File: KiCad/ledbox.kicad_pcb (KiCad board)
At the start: 2 copper layers, 80 x 50 mm, 132 parts, among them CON401 AVR_ISP, J201 Bus, J301 IR LED, J302 Button, J401 Power, J402 Power, J403 Power, J404 Port D, J405 Port B, J406 Port C, J407 ADC6, J408 ADC7, J501 6.5V-12V, J502 5V, SW301 Reset, SW302 Push 1, SW303 Push 2, U201 ST485C, U301 ULN2003, U401 ATMEGA88-20AU, U501 AZ1117-5.0, Y401 DNP/20MHz

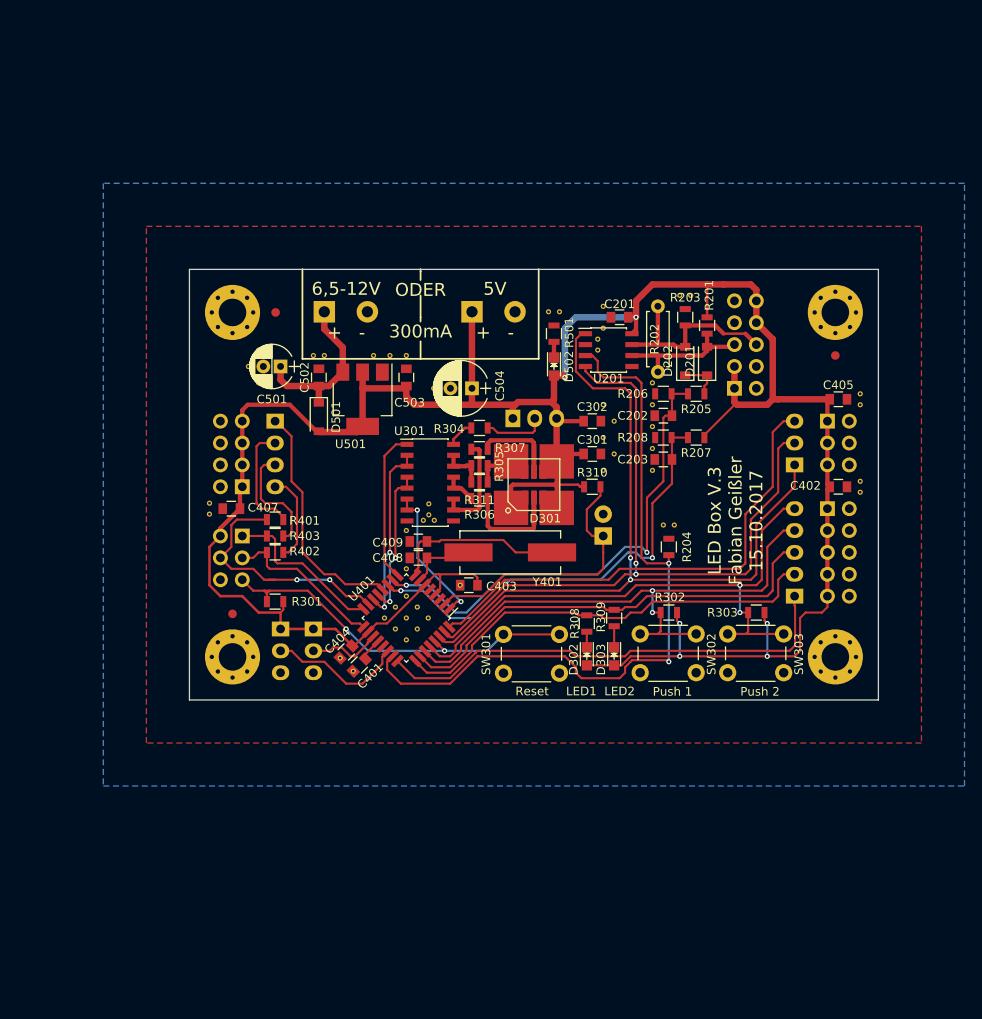
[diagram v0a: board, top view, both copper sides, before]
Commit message: Changes to V4 Schematic, new Board design
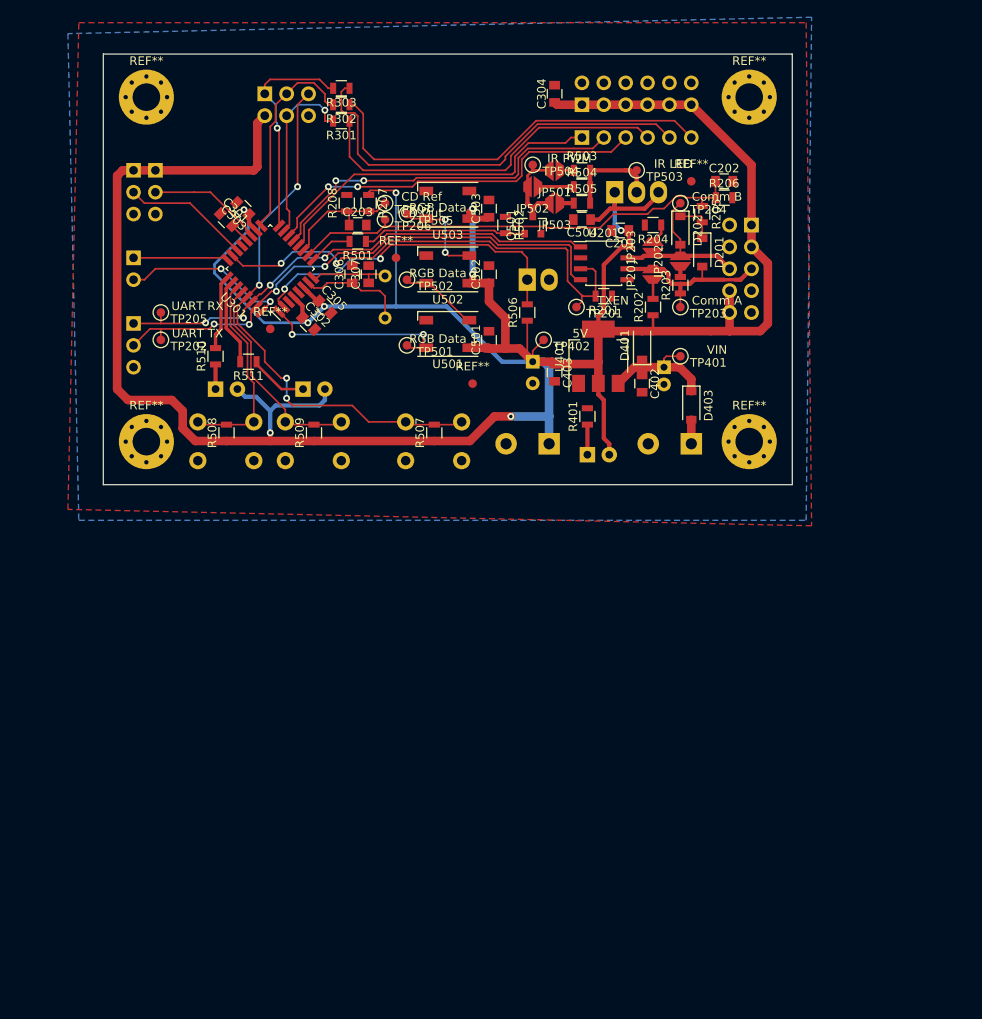
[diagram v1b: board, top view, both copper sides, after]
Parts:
- removed C405, C407: 100n, Capacitors_SMD:C_0805
- removed C408, C409: DNP/22p, Capacitors_SMD:C_0805
- removed CON401: AVR_ISP, Pin_Headers:Pin_Header_Straight_2x03
- removed D301: LRTBG6TG, ledbox-newfootprints:LED-6-BIG
- removed D302: LED1, LEDs:LED_0805
- removed D303: LED2, LEDs:LED_0805
- removed the G*** at (128.3, 101.3)
- removed the G*** at (150.0, 100.0)
- removed J403: Power, Socket_Strips:Socket_Strip_Straight_2x05
- removed J404: Port D, Socket_Strips:Socket_Strip_Straight_1x03
- removed J405: Port B, Socket_Strips:Socket_Strip_Straight_1x04
- removed J406: Port C, Socket_Strips:Socket_Strip_Straight_1x05
- removed J407: ADC6, Socket_Strips:Socket_Strip_Straight_1x03
- removed J408: ADC7, Socket_Strips:Socket_Strip_Straight_1x03
- removed R304: 150, Resistors_SMD:R_0805
- removed R305, R311: 82, Resistors_SMD:R_0805
- removed R306, R307: 22, Resistors_SMD:R_0805
- removed R308, R309: 430, Resistors_SMD:R_0805
- removed R310: 10k, Resistors_SMD:R_0805
- removed R402, R403: 1k, Resistors_SMD:R_0805
- removed the REF** at (138.4, 104.1)
- removed the REF** at (187.9, 99.6)
- removed the REF** at (187.9, 90.7)
- removed the REF** at (187.9, 89.5)
- removed the REF** at (163.8, 88.2)
- removed the REF** at (163.8, 90.7)
- removed the REF** at (163.8, 93.3)
- removed the REF** at (163.8, 95.8)
- removed the REF** at (163.8, 98.3)
- removed the REF** at (168.2, 78.0)
- removed the REF** at (166.9, 78.0)
- removed the REF** at (137.8, 102.2)
- removed the REF** at (158.0, 79.3)
- removed the REF** at (158.0, 81.8)
- removed the REF** at (153.0, 79.9)
- removed the REF** at (151.7, 79.9)
- removed the REF** at (157.4, 83.1)
- removed the REF** at (157.4, 84.4)
- removed the REF** at (158.0, 90.7)
- removed the REF** at (158.0, 98.3)
- removed the REF** at (158.0, 94.5)
- removed the REF** at (159.3, 96.4)
- removed the REF** at (137.8, 103.5)
- removed the REF** at (159.3, 92.6)
- removed the REF** at (141.4, 111.7)
- removed the REF** at (129.0, 121.7)
- removed the REF** at (127.5, 120.1)
- removed the REF** at (140.3, 86.9)
- removed the REF** at (125.7, 85.0)
- removed the REF** at (124.4, 85.0)
- removed the REF** at (135.2, 85.0)
- removed the REF** at (133.3, 85.0)
- removed the REF** at (131.4, 85.0)
- removed the REF** at (118.0, 88.2)
- removed the REF** at (138.4, 88.8)
- removed the REF** at (116.8, 86.3)
- removed the REF** at (118.0, 84.4)
- removed the REF** at (137.2, 104.1)
- removed the REF** at (135.2, 112.9)
- removed the REF** at (135.2, 105.3)
- removed the REF** at (135.2, 109.8)
- removed the REF** at (133.9, 114.2)
- removed the REF** at (136.5, 114.2)
- removed the REF** at (136.5, 116.8)
- removed the REF** at (112.3, 102.2)
- removed the REF** at (133.9, 116.8)
- removed the REF** at (135.2, 118.0)
- removed the REF** at (137.7, 115.5)
- removed the REF** at (132.6, 115.5)
- removed the REF** at (115.0, 115.0)
- removed the REF** at (185.0, 85.0)
- removed the REF** at (115.0, 80.0)
- removed the REF** at (115.0, 120.0)
- removed the REF** at (185.0, 120.0)
- removed the REF** at (185.0, 80.0)
- removed the REF** at (112.3, 103.4)
- removed the REF** at (120.0, 80.0)
- removed the REF** at (135.2, 115.5)
- removed the REF** at (166.3, 104.7)
- removed the REF** at (165.0, 104.7)
- removed the REF** at (187.9, 100.9)
- removed SW301: Reset, Buttons_Switches_THT:SW_PUSH_6mm_h5mm
- removed SW302: Push 1, Buttons_Switches_THT:SW_PUSH_6mm_h5mm
- removed SW303: Push 2, Buttons_Switches_THT:SW_PUSH_6mm_h5mm
- removed Y401: DNP/20MHz, Crystals:Crystal_HC49-SD_SMD
- added C303: 100n, Capacitors_SMD:C_0805, F.Cu at (116.2, 67.9)
- added C304: 100n, Capacitors_SMD:C_0805, F.Cu at (152.4, 54.6)
- added C305: 100n, Capacitors_SMD:C_0805, F.Cu at (125.7, 79.4)
- added C306: 22p, Capacitors_SMD:C_0805, F.Cu at (128.9, 75.6)
- added C307: 22p, Capacitors_SMD:C_0805, F.Cu at (130.8, 75.6)
- added CON301: AVR_ISP, Connectors_IDC:IDC-Header_2x03_Pitch2.54mm_Straight, B.Cu at (118.7, 54.6)
- added D401: 1N4148, Diodes_SMD:D_SOD-123, F.Cu at (162.6, 83.8)
- added D402: LED2, LEDs:LED_D3.0mm, B.Cu at (156.2, 96.5)
- added D403: PMEG4010ER, Diodes_SMD:D_SOD-123, F.Cu at (168.3, 90.8)
- added G***: LOGO, LOGO, B.Cu at (140.0, 75.0)
- added G***: LOGO, LOGO, F.Cu at (139.1, 56.5)
- added J303: Spare, Socket_Strips:Socket_Strip_Straight_1x02_Pitch2.54mm, B.Cu at (103.5, 73.7)
- added J304: UART, Socket_Strips:Socket_Strip_Straight_1x03_Pitch2.54mm, B.Cu at (103.5, 81.3)
- added J305: ADC6, Socket_Strips:Socket_Strip_Straight_1x03_Pitch2.54mm, B.Cu at (106.0, 63.5)
- added J306: ADC7, Socket_Strips:Socket_Strip_Straight_1x03_Pitch2.54mm, B.Cu at (103.5, 63.5)
- added JP201: COMMA PU, SMD_Jumper:Jumper_SMD_02, F.Cu at (163.8, 75.6)
- added JP202: TERM, SMD_Jumper:Jumper_SMD_02, F.Cu at (167.0, 74.0)
- added JP203: COMMB PD, SMD_Jumper:Jumper_SMD_02, F.Cu at (163.8, 72.4)
- added JP501: IR 12mA, SMD_Jumper:Jumper_SMD_02, F.Cu at (152.4, 63.5)
- added JP502: IR 24mA, SMD_Jumper:Jumper_SMD_02, F.Cu at (149.9, 65.4)
- added JP503: IR 48mA, SMD_Jumper:Jumper_SMD_02, F.Cu at (152.4, 67.3)
- added Q501: NTR4003N, TO_SOT_Packages_SMD:SOT-23, F.Cu at (149.9, 69.8)
- added R502: 100k, Resistors_SMD:R_0805, F.Cu at (146.7, 69.8)
- added R503: 300, Resistors_SMD:R_0805, F.Cu at (155.6, 63.5)
- added R504: 150, Resistors_SMD:R_0805, F.Cu at (155.6, 65.4)
- added R505: 75, Resistors_SMD:R_0805, F.Cu at (155.6, 67.3)
- added R506: 10k, Resistors_SMD:R_0805, F.Cu at (149.2, 80.0)
- added R507: 10k, Resistors_SMD:R_0805, F.Cu at (138.4, 94.0)
- added R508: 10k, Resistors_SMD:R_0805, F.Cu at (114.3, 94.0)
- added R509: 10k, Resistors_SMD:R_0805, F.Cu at (124.5, 94.0)
- added R510: 430, Resistors_SMD:R_0805, F.Cu at (113.0, 85.1)
- added R511: 430, Resistors_SMD:R_0805, F.Cu at (116.8, 85.7)
- added REF**: Fiducial_1mm_Dia_2mm_Outer, Fiducials:Fiducial_1mm_Dia_2mm_Outer, F.Cu at (168.3, 64.8)
- added REF**: Fiducial_1mm_Dia_2mm_Outer, Fiducials:Fiducial_1mm_Dia_2mm_Outer, F.Cu at (142.9, 88.3)
- added REF**: Fiducial_1mm_Dia_2mm_Outer, Fiducials:Fiducial_1mm_Dia_2mm_Outer, F.Cu at (119.4, 81.9)
- added REF**: Fiducial_1mm_Dia_2mm_Outer, Fiducials:Fiducial_1mm_Dia_2mm_Outer, F.Cu at (134.0, 73.7)
- added REF**: MountingHole_3.2mm_M3_Pad_Via, Mounting_Holes:MountingHole_3.2mm_M3_Pad_Via, F.Cu at (105.0, 95.0)
- added REF**: MountingHole_3.2mm_M3_Pad_Via, Mounting_Holes:MountingHole_3.2mm_M3_Pad_Via, F.Cu at (105.0, 55.0)
- added REF**: MountingHole_3.2mm_M3_Pad_Via, Mounting_Holes:MountingHole_3.2mm_M3_Pad_Via, F.Cu at (175.0, 55.0)
- added REF**: MountingHole_3.2mm_M3_Pad_Via, Mounting_Holes:MountingHole_3.2mm_M3_Pad_Via, F.Cu at (175.0, 95.0)
- added SW501: Reset, Buttons_Switches_THT:SW_PUSH_6mm_h5mm, B.Cu at (141.6, 92.7)
- added SW502: Push 1, Buttons_Switches_THT:SW_PUSH_6mm_h5mm, B.Cu at (117.5, 92.7)
- added SW503: Push 2, Buttons_Switches_THT:SW_PUSH_6mm_h5mm, B.Cu at (127.6, 92.7)
- added TP201: TXEN, Test:TEST_10, F.Cu at (154.9, 79.4)
- added TP202: UART TX, Test:TEST_10, F.Cu at (106.7, 83.2)
- added TP203: Comm A, Test:TEST_10, F.Cu at (167.0, 79.4)
- added TP204: Comm B, Test:TEST_10, F.Cu at (167.0, 67.3)
- added TP205: UART RX, Test:TEST_10, F.Cu at (106.7, 80.0)
- added TP206: CD Out, Test:TEST_10, F.Cu at (132.7, 69.2)
- added TP207: CD Ref, Test:TEST_10, F.Cu at (132.7, 67.3)
- added TP401: VIN, Test:TEST_10, F.Cu at (167.0, 85.1)
- added TP402: 5V, Test:TEST_10, F.Cu at (151.1, 83.2)
- added TP501: RGB Data 1, Test:TEST_10, F.Cu at (135.3, 83.8)
- added TP502: RGB Data 2, Test:TEST_10, F.Cu at (135.3, 76.2)
- added TP503: IR LED, Test:TEST_10, F.Cu at (161.9, 63.5)
- added TP504: IR PWM, Test:TEST_10, F.Cu at (149.9, 62.9)
- added TP505: RGB Data 3, Test:TEST_10, F.Cu at (135.3, 68.6)
- added U502: WS2812B, LEDs:LED_WS2812B-PLCC4, F.Cu at (140.0, 75.0)
- added U503: WS2812B, LEDs:LED_WS2812B-PLCC4, F.Cu at (140.0, 67.5)
- added Y301: 20MHz, Crystals:Crystal_HC49-U_Vertical, B.Cu at (132.7, 80.6)
- C301: value 10u -> 100n
- C401: value 100n -> 4u7; footprint Capacitors_SMD:C_0805 -> Capacitors_THT:CP_Radial_D5.0mm_P2.00mm; moved to B.Cu
- C404: value 100n -> 47u; footprint Capacitors_SMD:C_0805 -> Capacitors_THT:CP_Radial_D6.3mm_P2.50mm; moved to B.Cu
- C501: value 4u7 -> 10u; footprint Capacitors_THT:CP_Radial_D5.0mm_P2.00mm -> Capacitors_SMD:C_0805
- C502, C503: value 100n -> 10u
- C504: value 47u -> 100n; footprint Capacitors_THT:CP_Radial_D6.3mm_P2.50mm -> Capacitors_SMD:C_0805
- D501: value 1N4148 -> LED1; footprint Diodes_SMD:D_SOD-123 -> LEDs:LED_D3.0mm; moved to B.Cu
- D502: footprint LEDs:LED_0805 -> LEDs:LED_D3.0mm; moved to B.Cu
- J201: footprint Pin_Headers:Pin_Header_Straight_2x05 -> Connectors_IDC:IDC-Header_2x05_Pitch2.54mm_Straight
- J301: value IR LED -> Power B; footprint Pin_Headers:Pin_Header_Straight_1x03 -> Socket_Strips:Socket_Strip_Straight_2x06_Pitch2.54mm
- J302: value Button -> Port B; footprint Pin_Headers:Pin_Header_Straight_1x02 -> Socket_Strips:Socket_Strip_Straight_1x06_Pitch2.54mm
- J401: value Power -> 6.5V-12V; footprint Socket_Strips:Socket_Strip_Straight_2x03 -> TerminalBlock_MetzConnect:TerminalBlock_MetzConnect_Type055_RT01502HDWU_Pitch5.00mm
- J402: value Power -> 5V; footprint Socket_Strips:Socket_Strip_Straight_2x04 -> TerminalBlock_MetzConnect:TerminalBlock_MetzConnect_Type055_RT01502HDWU_Pitch5.00mm
- J501: value 6.5V-12V -> IR LED; footprint Connectors_Terminal_Blocks:TerminalBlock_Pheonix_MKDS1.5-2pol -> Connectors_Molex:Molex_KK-6410-03_03x2.54mm_Straight
- J502: value 5V -> Button; footprint Connectors_Terminal_Blocks:TerminalBlock_Pheonix_MKDS1.5-2pol -> Connectors_Molex:Molex_KK-6410-02_02x2.54mm_Straight
- R201: value DNP/1k -> 10k
- R202: value DNP/150 -> 1k; footprint Resistors_THT:R_Axial_DIN0207_L6.3mm_D2.5mm_P7.62mm_Horizontal -> Resistors_SMD:R_0805
- R203: value DNP/1k -> 150
- R204, R301, R302, R303: value 10k -> 1k
- R401: value 1k -> 2k2
- R501: value 430 -> 100
- U301: value ULN2003 -> ATMEGA88A-AU; footprint Housings_SOIC:SOIC-16_3.9x9.9mm_Pitch1.27mm -> Housings_QFP:TQFP-32_7x7mm_Pitch0.8mm
- U401: value ATMEGA88-20AU -> AZ1117-5.0; footprint Housings_QFP:TQFP-32_7x7mm_Pitch0.8mm -> TO_SOT_Packages_SMD:SOT-223-3_TabPin2
- U501: value AZ1117-5.0 -> WS2812B; footprint TO_SOT_Packages_SMD:SOT-223-3Lead_TabPin2 -> LEDs:LED_WS2812B-PLCC4
- moved R303 77.6 mm to (127.6, 54.0)
- moved R302 70.2 mm to (127.6, 55.9)
- moved R301 56.3 mm to (127.6, 57.8)
- moved C301 50.4 mm to (114.3, 69.2), turned to 315 degrees
- moved C401 49.5 mm to (165.1, 86.4), turned to 270 degrees
- moved R207 46.8 mm to (130.8, 67.3), turned to 270 degrees
- moved J302 46.3 mm to (155.6, 59.7), turned to 270 degrees
- moved R208 45.7 mm to (128.3, 67.3), turned to 90 degrees
- moved C203 44.7 mm to (129.5, 69.8), turned to 0 degrees
- moved C404 40.1 mm to (149.9, 85.7), turned to 270 degrees
- moved R401 38.2 mm to (156.2, 92.1), turned to 90 degrees
- moved U401 37.7 mm to (157.5, 85.1), turned to 90 degrees
- moved R204 37.4 mm to (163.8, 69.8), turned to 180 degrees
- moved J301 37.3 mm to (155.6, 55.9)
- moved J501 36.5 mm to (159.4, 66.0)
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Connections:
- C301 pad 1: +5V -> GND
- C301 pad 2: GND -> Net-(C301-Pad2)
- C401 pad 1: GND -> +12V
- C401 pad 2: Net-(C401-Pad2) -> GND
- C402 pad 1: +5V -> +12V
- C501 pad 1: +12V -> +5V
- C502 pad 1: +12V -> +5V
- D501 pad 1: +12V -> Net-(D501-Pad1)
- J301 pad 2: /Interface/IR_LED_DRV -> GND
- J302 pad 1: /Controller/BTN -> /Controller/PB0
- J302 pad 2: GND -> /Controller/PB1
- J401 pad 1: +5V -> Net-(D403-Pad2)
- J501 pad 1: +12V -> +5V
- J501 pad 2: GND -> /Interface/IR_LED_DRV
- J502 pad 1: +5V -> /Controller/BTN
- R201 pad 1: +5V -> GND
- R201 pad 2: /Bus/COMM_A -> /Bus/TX_EN
- R202 pad 1: /Bus/COMM_A -> +5V
- R202 pad 2: /Bus/COMM_B -> Net-(JP201-Pad1)
- R203 pad 1: /Bus/COMM_B -> /Bus/COMM_A
- R203 pad 2: GND -> Net-(JP202-Pad1)
- R204 pad 1: GND -> Net-(JP203-Pad2)
- R204 pad 2: /Bus/TX_EN -> GND
- R301 pad 1: +5V -> /Controller/PB3
- R301 pad 2: /Controller/~RESET -> /Controller/MOSI
- R302 pad 1: +5V -> /Controller/PB5
- R302 pad 2: /Controller/PUSH1 -> /Controller/SCK
- R303 pad 1: +5V -> /Controller/PB4
- R303 pad 2: /Controller/PUSH2 -> /Controller/MISO
- R401 pad 1: /Controller/PB3 -> Net-(D402-Pad1)
- R401 pad 2: /Controller/MOSI -> GND
- R501 pad 1: Net-(D502-Pad1) -> Net-(Q501-Pad1)
- R501 pad 2: GND -> /Controller/LED_IR
- U301 pad 1: /Controller/LED_IR -> /Controller/RGB_D
- U301 pad 10: Net-(R307-Pad2) -> /Bus/AIN0
- U301 pad 11: Net-(R307-Pad2) -> /Bus/AIN1
- U301 pad 12: Net-(R306-Pad2) -> /Controller/PB0
- U301 pad 13: Net-(R306-Pad2) -> /Controller/PB1
- U301 pad 14: Net-(R305-Pad2) -> /Controller/PB2
- U301 pad 15: Net-(R305-Pad2) -> /Controller/MOSI
- U301 pad 16: Net-(R304-Pad2) -> /Controller/MISO
- U301 pad 2: /Controller/PWM_R -> /Controller/BTN
- U301 pad 3: /Controller/PWM_R -> GND
- U301 pad 4: /Controller/PWM_G -> +5V
- U301 pad 5: /Controller/PWM_G -> GND
- U301 pad 6: /Controller/PWM_B -> +5V
- U301 pad 7: /Controller/PWM_B -> /Controller/XTAL1
- U301 pad 8: GND -> /Controller/XTAL2
- U301 pad 9: Net-(U301-Pad9) -> /Controller/LED_IR
- U401 pad 1: /Controller/PWM_B -> GND
- U401 pad 2: /Controller/BTN -> +5V
- U401 pad 3: GND -> +12V
- U501 pad 1: GND -> +5V
- U501 pad 2: +5V -> Net-(TP502-Pad1)
- U501 pad 3: +12V -> GND
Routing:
- net +5V: track 301.7 -> 373.8 mm, vias 6 -> 9
- net /Controller/PB2: track 0.00 -> 45.6 mm, vias 0 -> 2
- net /Controller/PC1: track 54.8 -> 11.0 mm
- net /Controller/PB1: track 0.00 -> 43.3 mm, vias 0 -> 2
- net /Controller/LED1: track 51.4 -> 8.75 mm
- net /Controller/PUSH2: track 66.9 -> 24.7 mm, vias 2 -> 0
- net /Controller/LED2: track 52.0 -> 10.2 mm
- net /Controller/PUSH1: track 65.3 -> 23.8 mm, vias 2 -> 0
- net /Bus/AIN1: track 52.6 -> 14.4 mm, vias 2 -> 0
- net /Controller/PD2: track 57.1 -> 19.6 mm, vias 0 -> 2
- net /Controller/PB5: track 10.4 -> 47.4 mm
- net /Controller/PB4: track 13.1 -> 49.4 mm
- net /Bus/RX: track 89.0 -> 58.6 mm, vias 2 -> 4
- net /Controller/PB3: track 13.0 -> 42.5 mm
- net /Bus/TX_EN: track 84.0 -> 56.5 mm
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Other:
- net class Default: via_dia 0.6 -> 0.8; via_drill 0.3 -> 0.4
- rule pad_to_mask_clearance: 0.2 -> 0
- board text removed: "+ -"
- board text removed: "5V"
- board text removed: "6,5-12V"
- board text removed: "LED Box V.3 Fabian Geißler 15.10.2017"
- board text removed: "LfdNr Addr Test"
- board text removed: "ODER 300mA"

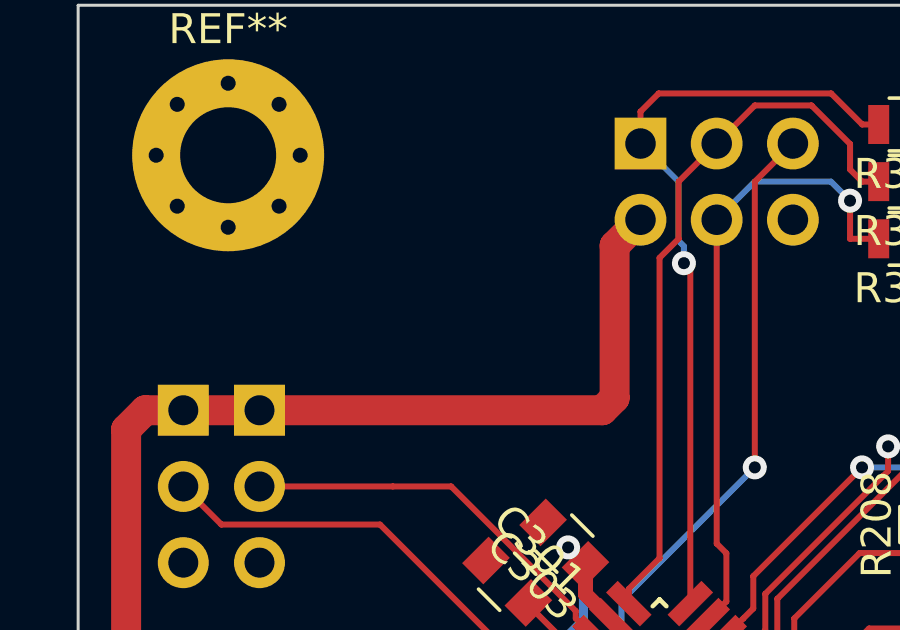
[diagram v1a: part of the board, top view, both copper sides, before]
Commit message: Added board plot
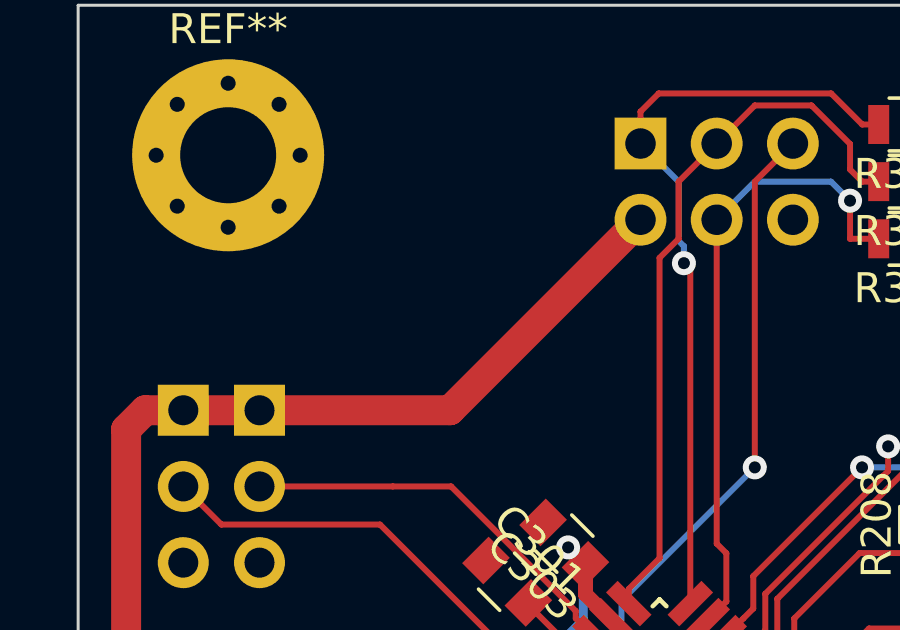
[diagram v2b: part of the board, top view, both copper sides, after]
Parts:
- moved G*** 1.07 mm to (140.0, 56.0)
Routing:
- net +5V: track 373.8 -> 370.8 mm
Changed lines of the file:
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@@
     (thickness 1.6)
     (drawings 4)
-    (tracks 595)
+    (tracks 593)
     (zones 0)
     (modules 101)
@@
   )
   (setup
-    (last_trace_width 0.2)
+    (last_trace_width 1)
     (user_trace_width 0.2)
     (user_trace_width 0.3)
@@
     (visible_elements FFFFFF7F)
     (pcbplotparams
-      (layerselection 0x010fc_ffffffff)
+      (layerselection 0x00000_ffffffff)
       (usegerberextensions false)
       (usegerberattributes true)
@@
       (padsonsilk false)
       (subtractmaskfromsilk false)
-      (outputformat 1)
+      (outputformat 4)
       (mirror false)
-      (drillshape 1)
+      (drillshape 0)
       (scaleselection 1)
-      (outputdirectory ""))
+      (outputdirectory output))
   )
   (net 0 "")
@@
   )
   (module LOGO (layer F.Cu)
-    (at 139.065 56.515)
+    (at 140 56)
     (fp_text reference G*** (at 0 0) (layer F.SilkS) hide
       (effects (font (thickness 0.3)))
@@
   (gr_line (start 180 50) (end 180 100) (layer Edge.Cuts) (width 0.1))
   (gr_line (start 100 50) (end 180 50) (layer Edge.Cuts) (width 0.1))
+  (segment (start 118.745 57.15) (end 112.395 63.5) (width 1) (layer F.Cu) (net 1))
+  (segment (start 112.395 63.5) (end 106.045 63.5) (width 1) (layer F.Cu) (net 1))
   (segment (start 151.13 83.185) (end 149.86 84.455) (width 0.2) (layer F.Cu) (net 1))
   (segment (start 149.86 84.455) (end 149.86 85.725) (width 0.2) (layer F.Cu) (net 1))
@@
   (segment (start 114.3 94.93) (end 119.38 94.93) (width 1) (layer F.Cu) (net 1))
   (segment (start 106.045 63.5) (end 103.505 63.5) (width 1) (layer F.Cu) (net 1))
-  (segment (start 117.881401 63.093599) (end 117.475 63.5) (width 1) (layer F.Cu) (net 1))
-  (segment (start 117.475 63.5) (end 106.045 63.5) (width 1) (layer F.Cu) (net 1))
-  (segment (start 118.745 57.15) (end 117.881401 58.013599) (width 1) (layer F.Cu) (net 1))
-  (segment (start 117.881401 58.013599) (end 117.881401 63.093599) (width 1) (layer F.Cu) (net 1))
   (segment (start 117.78901 70.510583) (end 116.912107 69.63368) (width 0.5) (layer F.Cu) (net 1))
   (segment (start 116.912107 69.63368) (end 116.912107 68.652107) (width 0.5) (layer F.Cu) (net 1))

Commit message: Finished v4 board
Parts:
- added G***: LOGO, LOGO, F.Cu at (139.0, 89.0)
- TP501: value RGB Data 1 -> RGB1
- TP502: value RGB Data 2 -> RGB2
- TP505: value RGB Data 3 -> RGB3
- U503: value WS2812B -> 3xWS2812B
- moved REF** 10.0 mm to (152.4, 91.4)
- moved REF** 7.25 mm to (133.6, 66.4)
- moved R207 4.44 mm to (126.7, 69.1)
- moved TP207 4.38 mm to (128.5, 66.0)
- moved J303 2.54 mm to (106.0, 73.7)
- moved J304 2.54 mm to (106.0, 81.3)
- moved J306 2.54 mm to (106.0, 63.5)
- moved J305 2.54 mm to (108.6, 63.5)
- moved TP202 2.54 mm to (109.2, 83.2)
- moved TP205 2.54 mm to (109.2, 80.0)
- moved TP401 2.01 mm to (165.1, 84.5)
- moved TP201 1.42 mm to (155.6, 78.1)
- moved R208 1.42 mm to (129.5, 67.9), turned to 0 degrees
- moved TP402 1.42 mm to (149.9, 83.8)
- moved TP206 0.65 mm to (133.3, 69.1)
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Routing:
- net +5V: track 370.8 -> 338.5 mm, vias 9 -> 10
- net /Controller/PD2: track 19.6 -> 14.5 mm
- net /Bus/AIN1: track 14.4 -> 10.4 mm
- net /Controller/PC1: track 11.0 -> 8.45 mm
- net /Controller/ADC7: track 14.8 -> 12.3 mm
- net /Controller/ADC6: track 13.4 -> 10.9 mm
- net /Controller/RGB_D: track 22.6 -> 20.2 mm, vias 2 -> 0
- net /Bus/TX: track 63.5 -> 61.9 mm
- net /Controller/PB1: track 43.3 -> 42.0 mm
- net /Controller/PB2: track 45.6 -> 44.4 mm
- net +12V: track 16.1 -> 15.0 mm
- net /Controller/PB0: track 40.2 -> 39.1 mm
- net /Controller/PB5: track 47.4 -> 48.3 mm
- net /Bus/TX_EN: track 56.5 -> 57.4 mm, vias 2 -> 4
- net /Bus/RX: track 58.6 -> 57.8 mm
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- added copper zone on F.Cu, net +5V
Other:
- net class Default: trace_width 0.25 -> 0.2; via_dia 0.8 -> 0.6; via_drill 0.4 -> 0.3
- board text added: "+"
- board text added: "-"
- board text added: "5V"

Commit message: Added version label
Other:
- board text added: "LED Box V.4 F. Geissler 15.03.2018"
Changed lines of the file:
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@@
   (general
     (thickness 1.6)
-    (drawings 38)
+    (drawings 39)
     (tracks 714)
     (zones 0)
@@
   (page A4)
   (layers
-    (0 F.Cu signal)
-    (31 B.Cu signal)
+    (0 F.Cu signal hide)
+    (31 B.Cu signal hide)
     (32 B.Adhes user)
     (33 F.Adhes user)
@@
     )
   )
+  (gr_text "LED Box V.4\nF. Geissler\n15.03.2018" (at 117.1575 61.7855) (layer F.SilkS)
+    (effects (font (size 1.2 1.2) (thickness 0.25)))
+  )
   (gr_line (start 171.323 84.582) (end 174.117 84.582) (layer F.SilkS) (width 0.2))
